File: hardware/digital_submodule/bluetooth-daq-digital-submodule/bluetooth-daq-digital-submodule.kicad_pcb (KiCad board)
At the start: 2 copper layers, 164 parts, among them J1 MCU I/F, J2 Digital Inputs, J3 Digital Outputs, J4 Communication I/F, J5 RS-485 I/F, U1 74HC595, U2 74HC595, U3 74HC165, U4 74HC165, U5 24LC1025, U6 SN75176AD, U7 CD4053B, U8 CD4053B

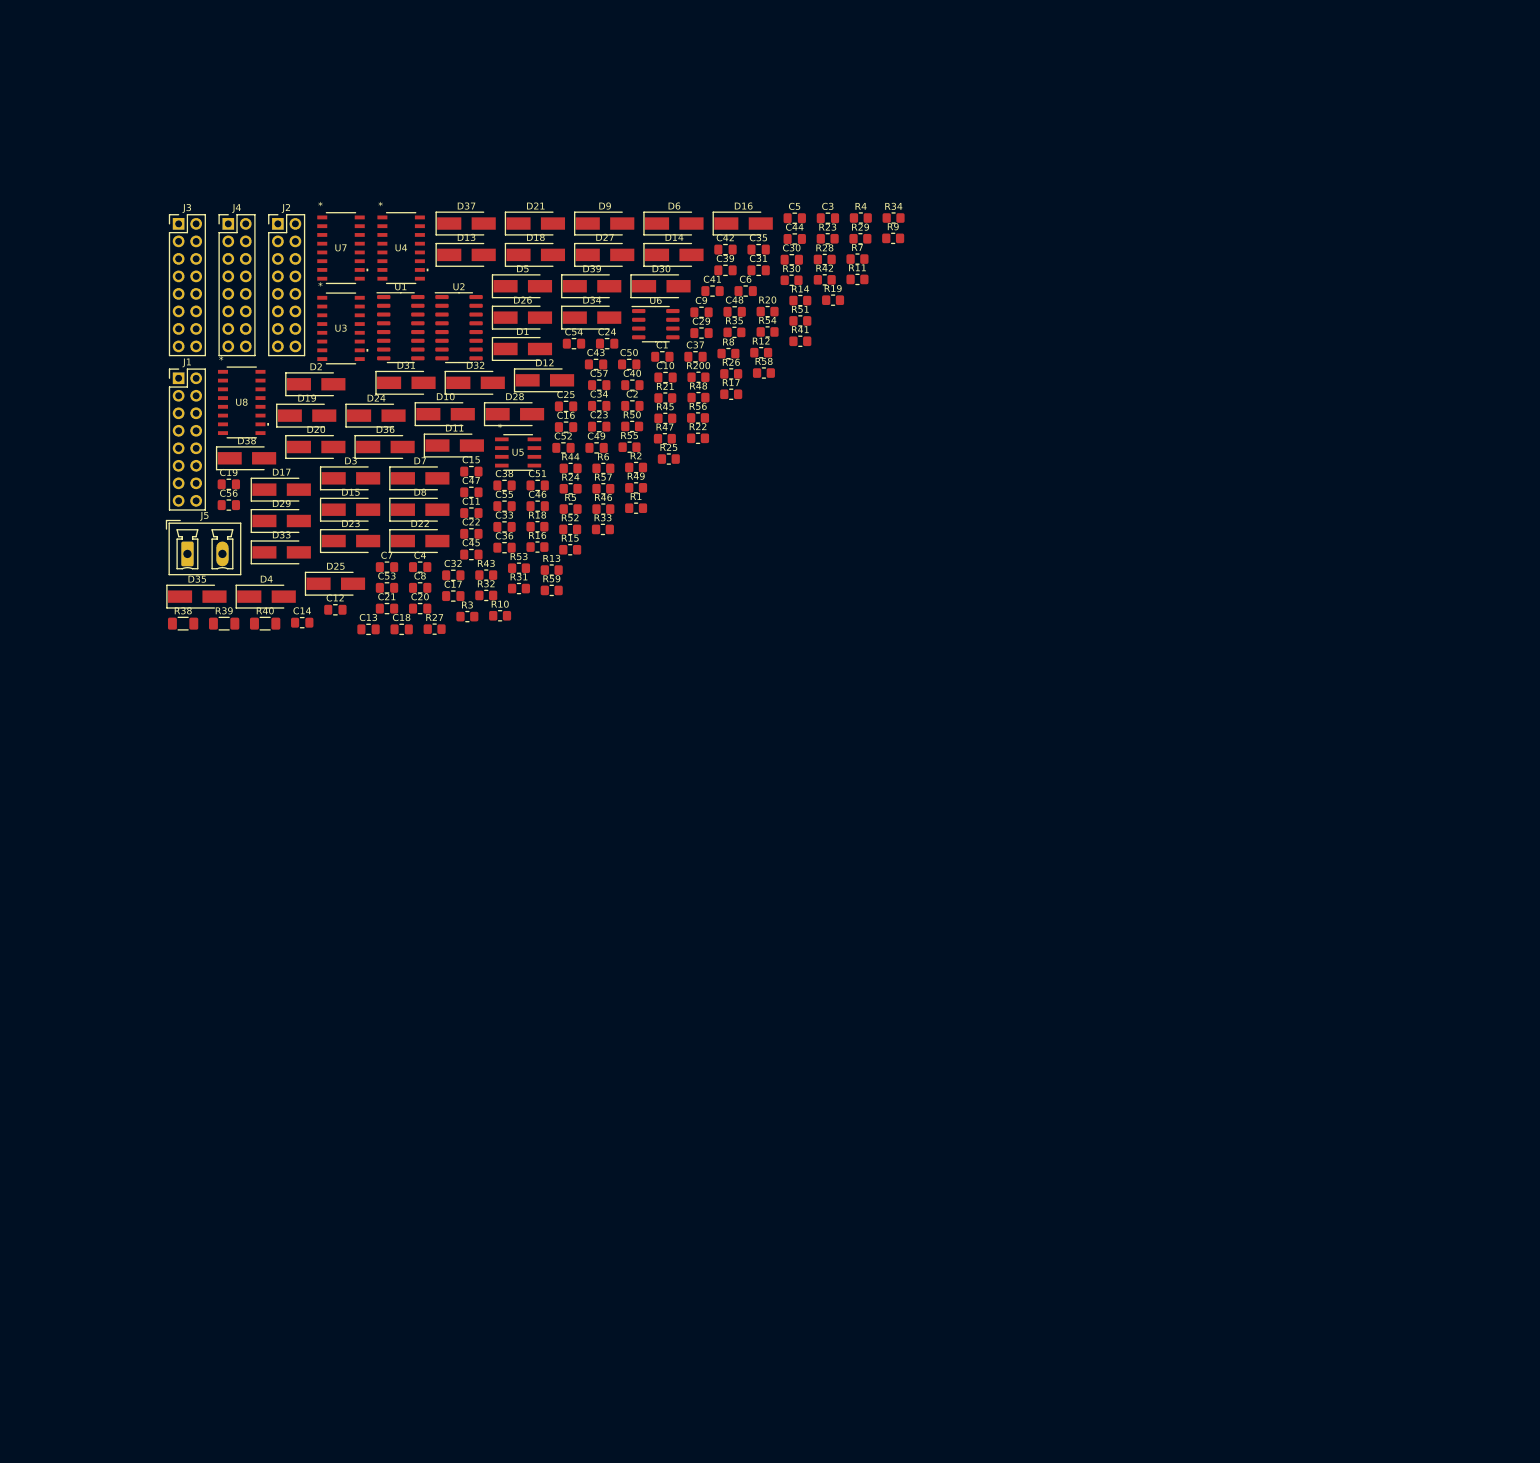
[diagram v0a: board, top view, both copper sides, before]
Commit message: Arranged components in PCB view according their functionality
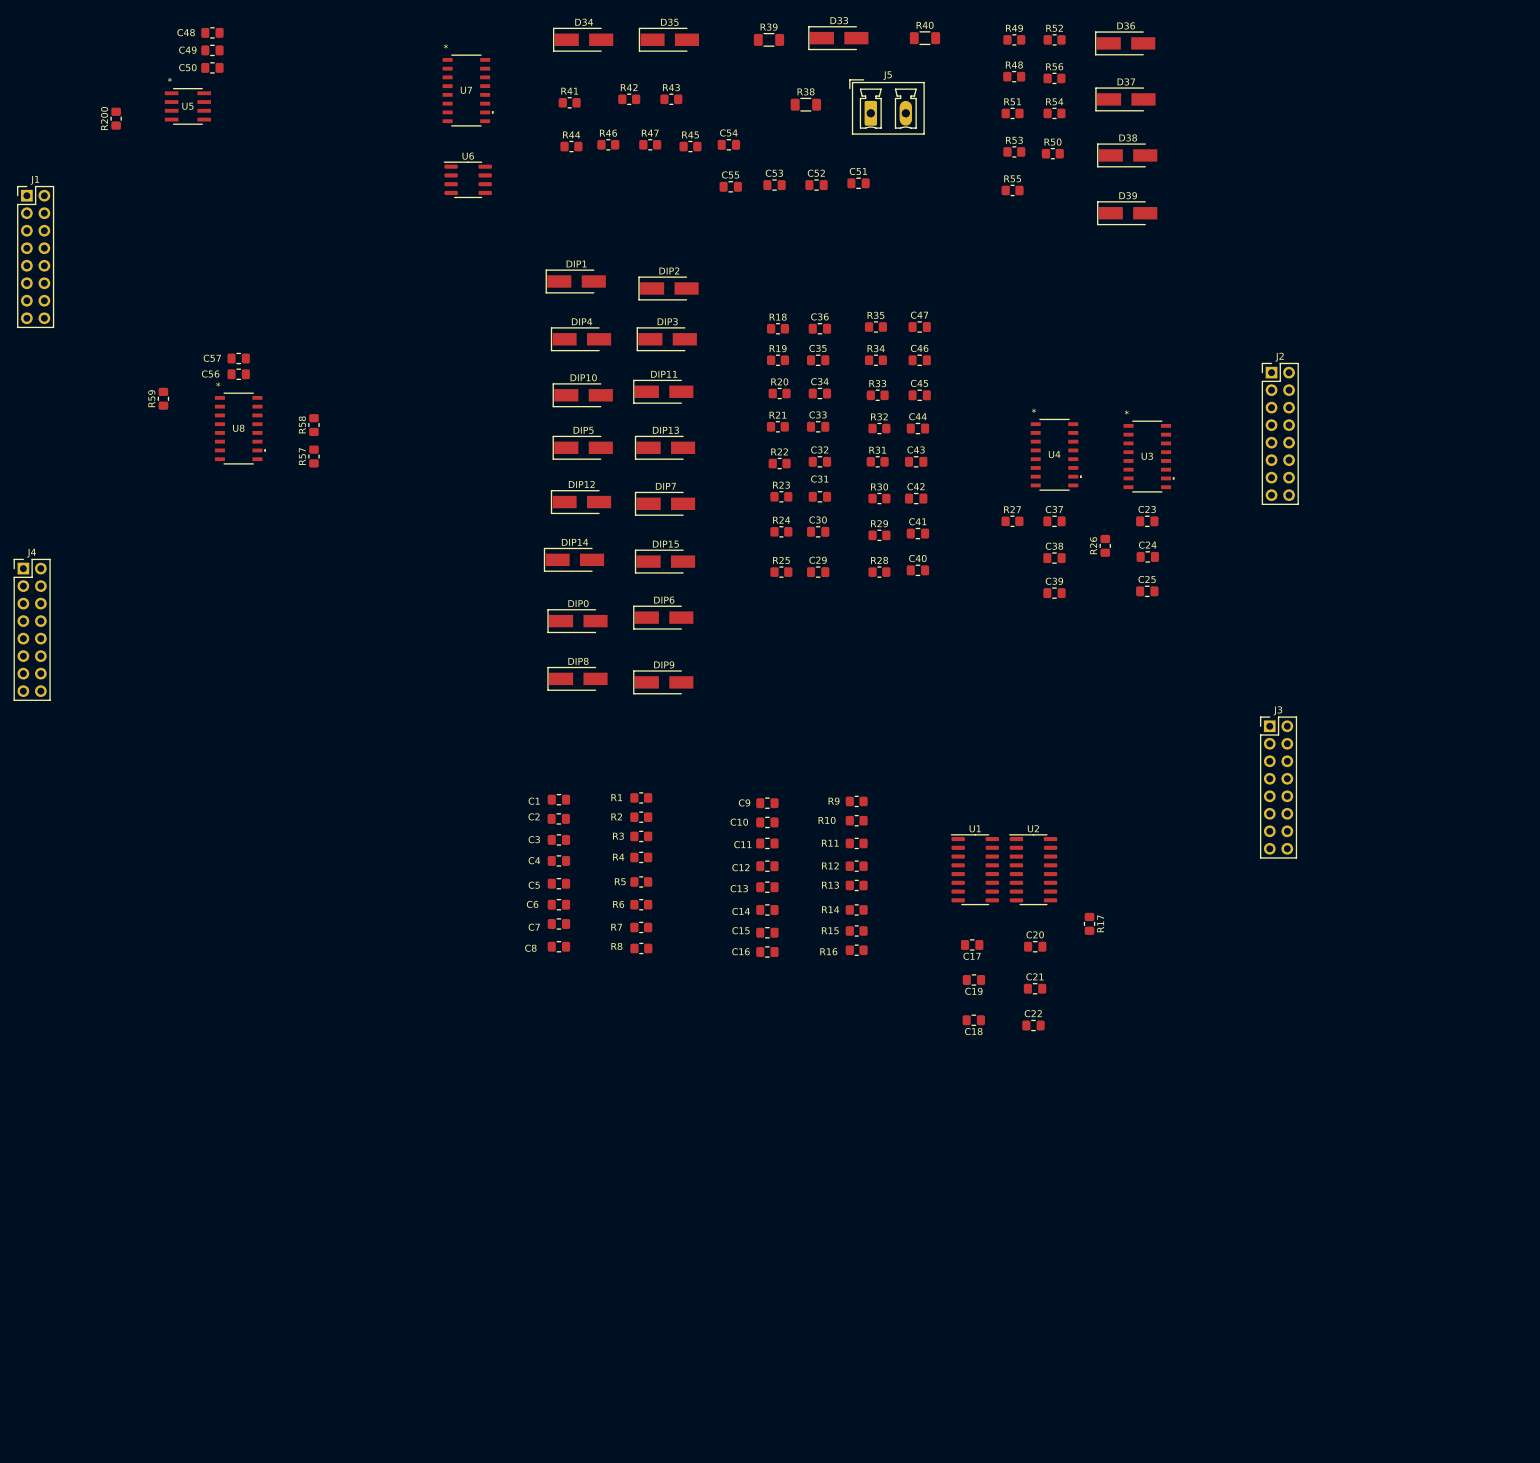
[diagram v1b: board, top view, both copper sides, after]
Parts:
- removed D1, D10, D11, D12, D13, D14, D15, D16, D17, D18, D19, D2, D20, D21, D22, D23, D24, D25, D26, D27, D28, D29, D3, D30, D31, D32, D4, D5, D6, D7, D8, D9: SMAJ5.0CA, Diode_SMD:D_SMA_Handsoldering
- added DIP0: D_Schottky, Diode_SMD:D_SMA_Handsoldering, F.Cu at (109.7, 101.6)
- added DIP1: D_Schottky, Diode_SMD:D_SMA_Handsoldering, F.Cu at (109.5, 52.3)
- added DIP10: D_Schottky, Diode_SMD:D_SMA_Handsoldering, F.Cu at (110.5, 68.8)
- added DIP11: D_Schottky, Diode_SMD:D_SMA_Handsoldering, F.Cu at (122.2, 68.3)
- added DIP12: D_Schottky, Diode_SMD:D_SMA_Handsoldering, F.Cu at (110.2, 84.3)
- added DIP13: D_Schottky, Diode_SMD:D_SMA_Handsoldering, F.Cu at (122.4, 76.5)
- added DIP14: D_Schottky, Diode_SMD:D_SMA_Handsoldering, F.Cu at (109.2, 92.7)
- added DIP15: D_Schottky, Diode_SMD:D_SMA_Handsoldering, F.Cu at (122.4, 93.0)
- added DIP2: D_Schottky, Diode_SMD:D_SMA_Handsoldering, F.Cu at (122.9, 53.3)
- added DIP3: D_Schottky, Diode_SMD:D_SMA_Handsoldering, F.Cu at (122.7, 60.7)
- added DIP4: D_Schottky, Diode_SMD:D_SMA_Handsoldering, F.Cu at (110.2, 60.7)
- added DIP5: D_Schottky, Diode_SMD:D_SMA_Handsoldering, F.Cu at (110.5, 76.5)
- added DIP6: D_Schottky, Diode_SMD:D_SMA_Handsoldering, F.Cu at (122.2, 101.1)
- added DIP7: D_Schottky, Diode_SMD:D_SMA_Handsoldering, F.Cu at (122.4, 84.6)
- added DIP8: D_Schottky, Diode_SMD:D_SMA_Handsoldering, F.Cu at (109.7, 110.0)
- added DIP9: D_Schottky, Diode_SMD:D_SMA_Handsoldering, F.Cu at (122.2, 110.5)
- moved J3 174.3 mm to (210.1, 116.9)
- moved J2 145.8 mm to (210.3, 65.5)
- moved D38 135.2 mm to (189.5, 34.0)
- moved C19 129.8 mm to (167.1, 153.7), turned to 180 degrees
- moved R40 128.0 mm to (160.0, 17.0)
- moved D36 122.4 mm to (189.2, 17.8)
- moved U3 118.5 mm to (192.3, 77.7)
- moved J5 118.0 mm to (152.2, 27.9)
- moved R38 117.6 mm to (142.7, 26.7)
- moved R39 115.9 mm to (137.4, 17.3)
- moved U1 114.6 mm to (167.3, 137.7)
- moved U2 114.6 mm to (175.8, 137.7)
- moved D33 110.0 mm to (147.6, 17.0)
- moved C21 109.0 mm to (176.0, 154.9)
- moved C22 108.4 mm to (175.8, 160.3)
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
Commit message: Decided on component arangement for digital input and digital output sections of the digital submodule.
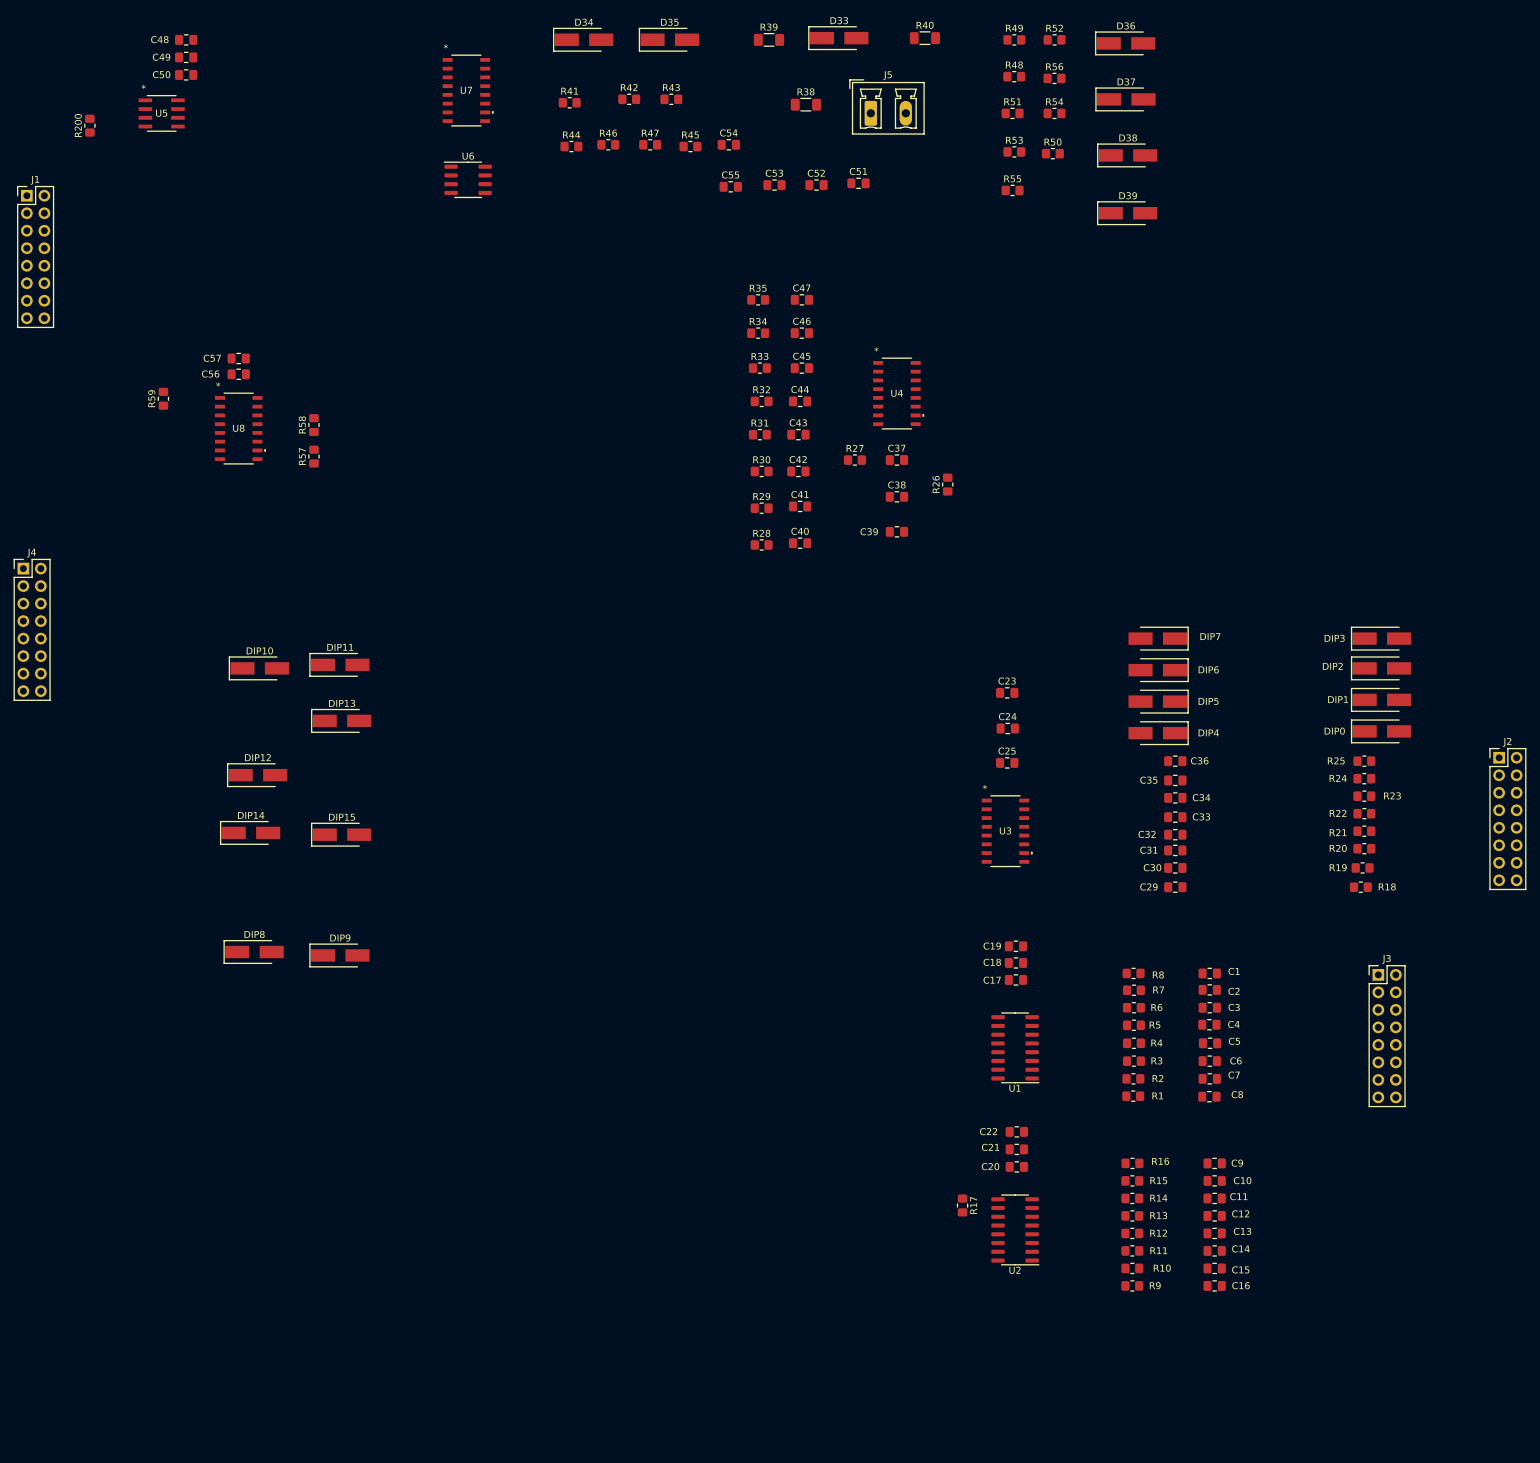
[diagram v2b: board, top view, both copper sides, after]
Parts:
- moved DIP1 131.7 mm to (226.3, 113.0)
- moved DIP0 117.7 mm to (226.3, 117.6)
- moved DIP2 117.2 mm to (226.3, 108.5)
- moved R18 117.1 mm to (223.3, 140.2), turned to 180 degrees
- moved DIP3 112.4 mm to (226.3, 104.1)
- moved R19 112.3 mm to (223.5, 137.4), turned to 180 degrees
- moved R20 107.5 mm to (223.8, 134.6), turned to 180 degrees
- moved R21 103.4 mm to (223.8, 132.1)
- moved DIP4 101.2 mm to (193.8, 117.9), turned to 180 degrees
- moved R22 98.9 mm to (223.8, 129.5), turned to 180 degrees
- moved C1 97.7 mm to (201.3, 152.7), turned to 180 degrees
- moved C2 97.7 mm to (201.3, 155.1), turned to 180 degrees
- moved C3 97.5 mm to (201.3, 157.7), turned to 180 degrees
- moved C4 97.3 mm to (201.3, 160.2), turned to 180 degrees
- moved C5 97.3 mm to (201.4, 162.9), turned to 180 degrees
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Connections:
- C29 pad 2: DIN0 -> Net-(R18-Pad2)
- C30 pad 2: DIN1 -> Net-(R19-Pad2)
- C31 pad 2: DIN2 -> Net-(R20-Pad2)
- C32 pad 2: DIN3 -> Net-(U3-Pad3)
- C33 pad 2: DIN4 -> Net-(R22-Pad2)
- C34 pad 2: DIN5 -> Net-(R23-Pad2)
- C35 pad 2: DIN6 -> Net-(U3-Pad12)
- C36 pad 2: DIN7 -> Net-(U3-Pad11)
- C40 pad 2: DIN15 -> Net-(R35-Pad2)
- C41 pad 2: DIN14 -> Net-(R34-Pad2)
- C42 pad 2: DIN13 -> Net-(R33-Pad2)
- C43 pad 2: DIN12 -> Net-(R32-Pad2)
- C44 pad 2: DIN11 -> Net-(R31-Pad2)
- C45 pad 2: DIN10 -> Net-(R30-Pad2)
- C46 pad 2: DIN9 -> Net-(R29-Pad2)
- C47 pad 2: DIN8 -> Net-(R28-Pad2)
- J3 pad 1: DOUT0 -> DOUT7
- J3 pad 10: DOUT12 -> DOUT11
- J3 pad 11: DOUT5 -> DOUT2
- J3 pad 12: DOUT13 -> DOUT10
- J3 pad 13: DOUT6 -> DOUT1
- J3 pad 14: DOUT14 -> DOUT9
- J3 pad 15: DOUT7 -> DOUT0
- J3 pad 16: DOUT15 -> DOUT8
- J3 pad 2: DOUT8 -> DOUT15
- J3 pad 3: DOUT1 -> DOUT6
- J3 pad 4: DOUT9 -> DOUT14
- J3 pad 5: DOUT2 -> DOUT5
- J3 pad 6: DOUT10 -> DOUT13
- J3 pad 7: DOUT3 -> DOUT4
- J3 pad 8: DOUT11 -> DOUT12
- J3 pad 9: DOUT4 -> DOUT3
